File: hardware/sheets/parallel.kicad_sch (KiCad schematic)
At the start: 37 parts, among them J1 DB25_Pins, U1 74HCT574, U10 74HCT32, U11 74HCT32, U12 74HCT00, U13 74HCT125, U2 74HCT574, U3 74HCT244, U4 74HCT245, U5 74HCT244, U6 74HCT138, U7 74HCT08, U8 74HCT08, U9 74HCT04

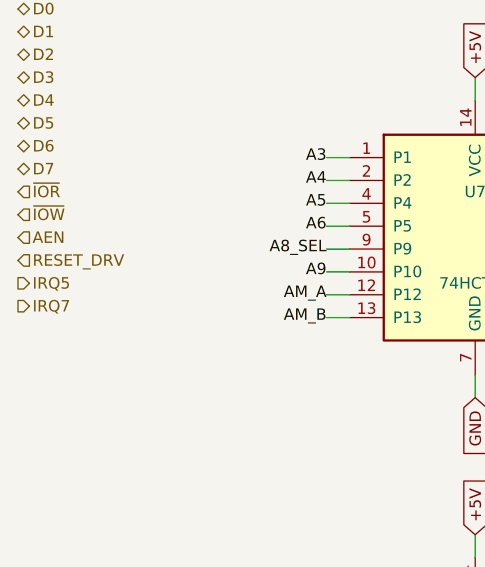
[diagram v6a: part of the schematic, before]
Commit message: Design-review fixes: reset parking, IRQ8 off the header, analog cleanups
Netlist-wide review sweep. IRQ8 leaves the 60-pin ISA header (pin 15 is a
second GND return; the on-board RTC owns IRQ8 exclusively, so its push-pull
drive is now correct by construction). Bus MCU Hi-Z parking completed:
~CPURESET pulled low (V20 held in reset while the MCU is unprogrammed),
~DACK1/~REFRESH parked deasserted, DRQ1 idled low. Supervisor 12 MHz crystal
damping R actually in series now (was parallel-to-nothing), plus a second
USBLC6 so both prog-port SW2 positions are ESD-protected. Audio: 0.5x PG
summing (MCP6002 headroom), 100k LINE bleed, unit B parked as a follower --
and the SUM stub moved off pin 5's row, where wiring unit B would have
silently merged SUM into VREF. CH224K VDD fed through 1k per the WCH ref
design. VGA blue ladder rescaled 1k/510 -> 820/470 (was ~12% blue-deficient).
Spare CMOS gate inputs grounded uniformly (cpu_core/rtc/storage); UART_RXD
pulled up (SIN idles at mark with JP1 open); dead pins/parts dropped
(com_port CLK, parallel RESET_DRV, storage R3). Bus CLK fixed at 7.16 MHz
logged as a decision. New passives mapped to JLC basic parts in parts.py.

Co-Authored-By: Claude Fable 5 <noreply@anthropic.com>
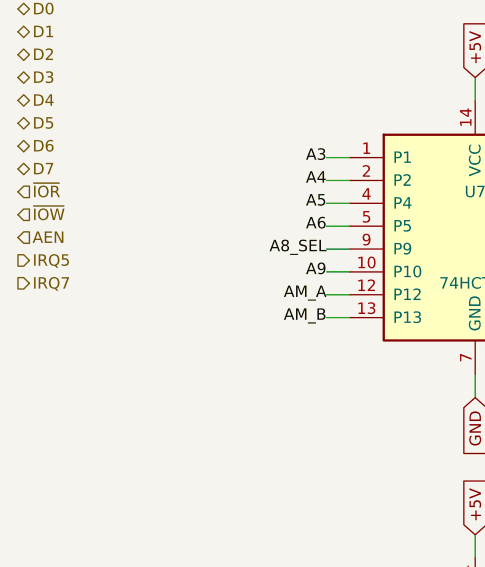
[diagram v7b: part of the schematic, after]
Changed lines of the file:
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@@
 		)
 	)
-	(hierarchical_label "RESET_DRV"
-		(shape input)
-		(at 25.4 78.74 0)
-		(effects
-			(font
-				(size 1.27 1.27)
-			)
-		)
-	)
 	(hierarchical_label "IRQ5"
 		(shape output)
-		(at 25.4 81.28 0)
+		(at 25.4 78.74 0)
 		(effects
 			(font
@@
 	(hierarchical_label "IRQ7"
 		(shape output)
-		(at 25.4 83.82 0)
+		(at 25.4 81.28 0)
 		(effects
 			(font
@@
 		(instances
 			(project "mini-xt"
-				(path "/26736c46-8b40-5460-874f-03596d17270c/905566e2-89a4-5528-a19b-779bf8cc21ad"
+				(path "/26736c46-8b40-5460-874f-03596d17270c/f978aad9-2605-50e7-930d-75b974709c1c"
 					(reference "U707")
 					(unit 1)
@@
 		(instances
 			(project "mini-xt"
-				(path "/26736c46-8b40-5460-874f-03596d17270c/905566e2-89a4-5528-a19b-779bf8cc21ad"
+				(path "/26736c46-8b40-5460-874f-03596d17270c/f978aad9-2605-50e7-930d-75b974709c1c"
 					(reference "U708")
 					(unit 1)
@@
 		(instances
 			(project "mini-xt"
-				(path "/26736c46-8b40-5460-874f-03596d17270c/905566e2-89a4-5528-a19b-779bf8cc21ad"
+				(path "/26736c46-8b40-5460-874f-03596d17270c/f978aad9-2605-50e7-930d-75b974709c1c"
 					(reference "U709")
 					(unit 1)
@@
 		(instances
 			(project "mini-xt"
-				(path "/26736c46-8b40-5460-874f-03596d17270c/905566e2-89a4-5528-a19b-779bf8cc21ad"
+				(path "/26736c46-8b40-5460-874f-03596d17270c/f978aad9-2605-50e7-930d-75b974709c1c"
 					(reference "U712")
 					(unit 1)
@@
 		(instances
 			(project "mini-xt"
-				(path "/26736c46-8b40-5460-874f-03596d17270c/905566e2-89a4-5528-a19b-779bf8cc21ad"
+				(path "/26736c46-8b40-5460-874f-03596d17270c/f978aad9-2605-50e7-930d-75b974709c1c"
 					(reference "U713")
 					(unit 1)
@@
 		(instances
 			(project "mini-xt"
-				(path "/26736c46-8b40-5460-874f-03596d17270c/905566e2-89a4-5528-a19b-779bf8cc21ad"
+				(path "/26736c46-8b40-5460-874f-03596d17270c/f978aad9-2605-50e7-930d-75b974709c1c"
 					(reference "U706")
 					(unit 1)
@@
 		(instances
 			(project "mini-xt"
-				(path "/26736c46-8b40-5460-874f-03596d17270c/905566e2-89a4-5528-a19b-779bf8cc21ad"
+				(path "/26736c46-8b40-5460-874f-03596d17270c/f978aad9-2605-50e7-930d-75b974709c1c"
 					(reference "U710")
 					(unit 1)
@@
 		(instances
 			(project "mini-xt"
-				(path "/26736c46-8b40-5460-874f-03596d17270c/905566e2-89a4-5528-a19b-779bf8cc21ad"
+				(path "/26736c46-8b40-5460-874f-03596d17270c/f978aad9-2605-50e7-930d-75b974709c1c"
 					(reference "U711")
 					(unit 1)
@@
 		(instances
 			(project "mini-xt"
-				(path "/26736c46-8b40-5460-874f-03596d17270c/905566e2-89a4-5528-a19b-779bf8cc21ad"
+				(path "/26736c46-8b40-5460-874f-03596d17270c/f978aad9-2605-50e7-930d-75b974709c1c"
 					(reference "U701")
 					(unit 1)
@@
 		(instances
 			(project "mini-xt"
-				(path "/26736c46-8b40-5460-874f-03596d17270c/905566e2-89a4-5528-a19b-779bf8cc21ad"
+				(path "/26736c46-8b40-5460-874f-03596d17270c/f978aad9-2605-50e7-930d-75b974709c1c"
 					(reference "U704")
 					(unit 1)
@@
 		(instances
 			(project "mini-xt"
-				(path "/26736c46-8b40-5460-874f-03596d17270c/905566e2-89a4-5528-a19b-779bf8cc21ad"
+				(path "/26736c46-8b40-5460-874f-03596d17270c/f978aad9-2605-50e7-930d-75b974709c1c"
 					(reference "U702")
 					(unit 1)
@@
 		(instances
 			(project "mini-xt"
-				(path "/26736c46-8b40-5460-874f-03596d17270c/905566e2-89a4-5528-a19b-779bf8cc21ad"
+				(path "/26736c46-8b40-5460-874f-03596d17270c/f978aad9-2605-50e7-930d-75b974709c1c"
 					(reference "U705")
 					(unit 1)
@@
 		(instances
 			(project "mini-xt"
-				(path "/26736c46-8b40-5460-874f-03596d17270c/905566e2-89a4-5528-a19b-779bf8cc21ad"
+				(path "/26736c46-8b40-5460-874f-03596d17270c/f978aad9-2605-50e7-930d-75b974709c1c"
 					(reference "U703")
 					(unit 1)
@@
 		(instances
 			(project "mini-xt"
-				(path "/26736c46-8b40-5460-874f-03596d17270c/905566e2-89a4-5528-a19b-779bf8cc21ad"
+				(path "/26736c46-8b40-5460-874f-03596d17270c/f978aad9-2605-50e7-930d-75b974709c1c"
 					(reference "J701")
 					(unit 1)
@@
 		(instances
 			(project "mini-xt"
-				(path "/26736c46-8b40-5460-874f-03596d17270c/905566e2-89a4-5528-a19b-779bf8cc21ad"
+				(path "/26736c46-8b40-5460-874f-03596d17270c/f978aad9-2605-50e7-930d-75b974709c1c"
 					(reference "R701")
 					(unit 1)
@@
 		(instances
 			(project "mini-xt"
-				(path "/26736c46-8b40-5460-874f-03596d17270c/905566e2-89a4-5528-a19b-779bf8cc21ad"
+				(path "/26736c46-8b40-5460-874f-03596d17270c/f978aad9-2605-50e7-930d-75b974709c1c"
 					(reference "R702")
 					(unit 1)
@@
 		(instances
 			(project "mini-xt"
-				(path "/26736c46-8b40-5460-874f-03596d17270c/905566e2-89a4-5528-a19b-779bf8cc21ad"
+				(path "/26736c46-8b40-5460-874f-03596d17270c/f978aad9-2605-50e7-930d-75b974709c1c"
 					(reference "R703")
 					(unit 1)
@@
 		(instances
 			(project "mini-xt"
-				(path "/26736c46-8b40-5460-874f-03596d17270c/905566e2-89a4-5528-a19b-779bf8cc21ad"
+				(path "/26736c46-8b40-5460-874f-03596d17270c/f978aad9-2605-50e7-930d-75b974709c1c"
 					(reference "R704")
 					(unit 1)
@@
 		(instances
 			(project "mini-xt"
-				(path "/26736c46-8b40-5460-874f-03596d17270c/905566e2-89a4-5528-a19b-779bf8cc21ad"
+				(path "/26736c46-8b40-5460-874f-03596d17270c/f978aad9-2605-50e7-930d-75b974709c1c"
 					(reference "R705")
 					(unit 1)
@@
 		(instances
 			(project "mini-xt"
-				(path "/26736c46-8b40-5460-874f-03596d17270c/905566e2-89a4-5528-a19b-779bf8cc21ad"
+				(path "/26736c46-8b40-5460-874f-03596d17270c/f978aad9-2605-50e7-930d-75b974709c1c"
 					(reference "JP701")
 					(unit 1)
@@
 		(instances
 			(project "mini-xt"
-				(path "/26736c46-8b40-5460-874f-03596d17270c/905566e2-89a4-5528-a19b-779bf8cc21ad"
+				(path "/26736c46-8b40-5460-874f-03596d17270c/f978aad9-2605-50e7-930d-75b974709c1c"
 					(reference "JP702")
 					(unit 1)
@@
 		(instances
 			(project "mini-xt"
-				(path "/26736c46-8b40-5460-874f-03596d17270c/905566e2-89a4-5528-a19b-779bf8cc21ad"
+				(path "/26736c46-8b40-5460-874f-03596d17270c/f978aad9-2605-50e7-930d-75b974709c1c"
 					(reference "R706")
 					(unit 1)
@@
 		(instances
 			(project "mini-xt"
-				(path "/26736c46-8b40-5460-874f-03596d17270c/905566e2-89a4-5528-a19b-779bf8cc21ad"
+				(path "/26736c46-8b40-5460-874f-03596d17270c/f978aad9-2605-50e7-930d-75b974709c1c"
 					(reference "JP703")
 					(unit 1)
@@
 		(instances
 			(project "mini-xt"
-				(path "/26736c46-8b40-5460-874f-03596d17270c/905566e2-89a4-5528-a19b-779bf8cc21ad"
+				(path "/26736c46-8b40-5460-874f-03596d17270c/f978aad9-2605-50e7-930d-75b974709c1c"
 					(reference "C701")
 					(unit 1)
@@
 		(instances
 			(project "mini-xt"
-				(path "/26736c46-8b40-5460-874f-03596d17270c/905566e2-89a4-5528-a19b-779bf8cc21ad"
+				(path "/26736c46-8b40-5460-874f-03596d17270c/f978aad9-2605-50e7-930d-75b974709c1c"
 					(reference "C702")
 					(unit 1)
@@
 		(instances
 			(project "mini-xt"
-				(path "/26736c46-8b40-5460-874f-03596d17270c/905566e2-89a4-5528-a19b-779bf8cc21ad"
+				(path "/26736c46-8b40-5460-874f-03596d17270c/f978aad9-2605-50e7-930d-75b974709c1c"
 					(reference "C703")
 					(unit 1)
@@
 		(instances
 			(project "mini-xt"
-				(path "/26736c46-8b40-5460-874f-03596d17270c/905566e2-89a4-5528-a19b-779bf8cc21ad"
+				(path "/26736c46-8b40-5460-874f-03596d17270c/f978aad9-2605-50e7-930d-75b974709c1c"
 					(reference "C704")
 					(unit 1)
@@
 		(instances
 			(project "mini-xt"
-				(path "/26736c46-8b40-5460-874f-03596d17270c/905566e2-89a4-5528-a19b-779bf8cc21ad"
+				(path "/26736c46-8b40-5460-874f-03596d17270c/f978aad9-2605-50e7-930d-75b974709c1c"
 					(reference "C705")
 					(unit 1)
@@
 		(instances
 			(project "mini-xt"
-				(path "/26736c46-8b40-5460-874f-03596d17270c/905566e2-89a4-5528-a19b-779bf8cc21ad"
+				(path "/26736c46-8b40-5460-874f-03596d17270c/f978aad9-2605-50e7-930d-75b974709c1c"
 					(reference "C706")
 					(unit 1)
@@
 		(instances
 			(project "mini-xt"
-				(path "/26736c46-8b40-5460-874f-03596d17270c/905566e2-89a4-5528-a19b-779bf8cc21ad"
+				(path "/26736c46-8b40-5460-874f-03596d17270c/f978aad9-2605-50e7-930d-75b974709c1c"
 					(reference "C707")
 					(unit 1)
@@
 		(instances
 			(project "mini-xt"
-				(path "/26736c46-8b40-5460-874f-03596d17270c/905566e2-89a4-5528-a19b-779bf8cc21ad"
+				(path "/26736c46-8b40-5460-874f-03596d17270c/f978aad9-2605-50e7-930d-75b974709c1c"
 					(reference "C708")
 					(unit 1)
@@
 		(instances
 			(project "mini-xt"
-				(path "/26736c46-8b40-5460-874f-03596d17270c/905566e2-89a4-5528-a19b-779bf8cc21ad"
+				(path "/26736c46-8b40-5460-874f-03596d17270c/f978aad9-2605-50e7-930d-75b974709c1c"
 					(reference "C709")
 					(unit 1)
@@
 		(instances
 			(project "mini-xt"
-				(path "/26736c46-8b40-5460-874f-03596d17270c/905566e2-89a4-5528-a19b-779bf8cc21ad"
+				(path "/26736c46-8b40-5460-874f-03596d17270c/f978aad9-2605-50e7-930d-75b974709c1c"
 					(reference "C710")
 					(unit 1)
@@
 		(instances
 			(project "mini-xt"
-				(path "/26736c46-8b40-5460-874f-03596d17270c/905566e2-89a4-5528-a19b-779bf8cc21ad"
+				(path "/26736c46-8b40-5460-874f-03596d17270c/f978aad9-2605-50e7-930d-75b974709c1c"
 					(reference "C711")
 					(unit 1)
@@
 		(instances
 			(project "mini-xt"
-				(path "/26736c46-8b40-5460-874f-03596d17270c/905566e2-89a4-5528-a19b-779bf8cc21ad"
+				(path "/26736c46-8b40-5460-874f-03596d17270c/f978aad9-2605-50e7-930d-75b974709c1c"
 					(reference "C712")
 					(unit 1)
@@
 		(instances
 			(project "mini-xt"
-				(path "/26736c46-8b40-5460-874f-03596d17270c/905566e2-89a4-5528-a19b-779bf8cc21ad"
+				(path "/26736c46-8b40-5460-874f-03596d17270c/f978aad9-2605-50e7-930d-75b974709c1c"
 					(reference "C713")
 					(unit 1)
@@
 		(instances
 			(project "mini-xt"
-				(path "/26736c46-8b40-5460-874f-03596d17270c/905566e2-89a4-5528-a19b-779bf8cc21ad"
+				(path "/26736c46-8b40-5460-874f-03596d17270c/f978aad9-2605-50e7-930d-75b974709c1c"
 					(reference "C714")
 					(unit 1)

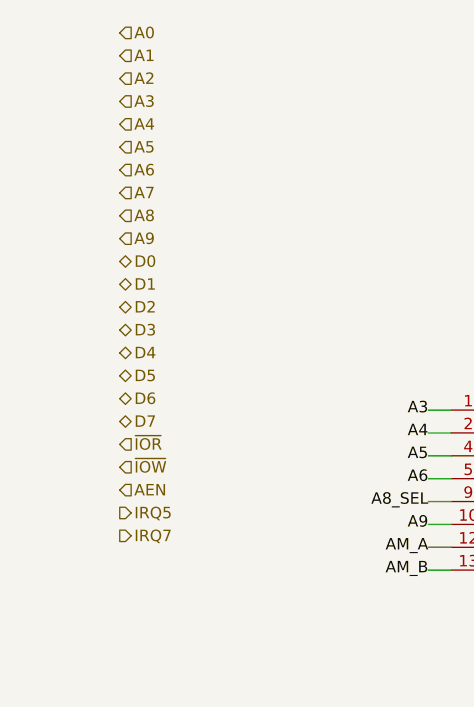
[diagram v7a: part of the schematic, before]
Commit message: ERC cleanup: NC flags on unused pins, anchored interface labels
KiCad 10 ERC drops from 366 to 16 violations, all noise:

- NC flags on the 36 genuinely unused pins (cpu_core '138/'161 spares,
  Supervisor RP2040 unused GPIO, Core2350B GPIO44-47, rtc '138 spares).
- emit_interface anchors every hier label on a stub wire ending in a
  same-name local label -- connectivity unchanged (still by name;
  netlist spans verified), but nothing dangles.
- Interface honesty: cpu_core drops AEN/IOCHRDY from PINS (both live on
  bus_mcu; nothing here touched them), bus_mcu drops PRIV_COUNTER (the
  counter chain is on-sheet, CNT_* never crosses).
- Remaining 6 label_dangling are root IRQ9-13/15: single-sheet by
  design (soft-PIC pull-ups await future 16-bit sources); kept in PINS
  as the AT-style contract.

Co-Authored-By: Claude Fable 5 <noreply@anthropic.com>
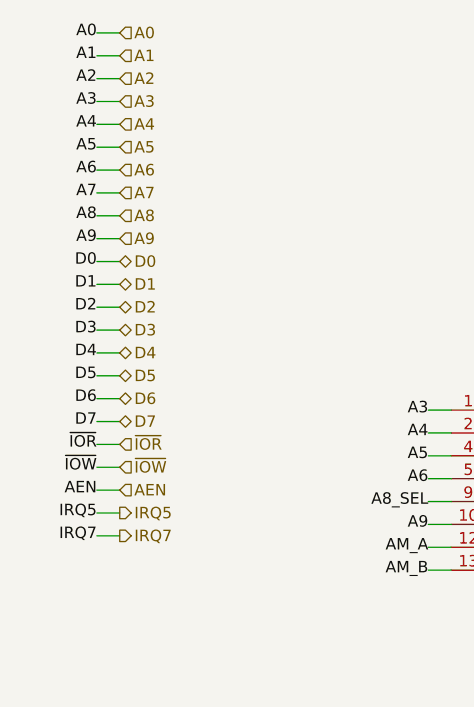
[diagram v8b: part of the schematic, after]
